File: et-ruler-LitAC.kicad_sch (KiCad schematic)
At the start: 26 parts, among them J1 Conn_01x03, SW1 SW_DPST

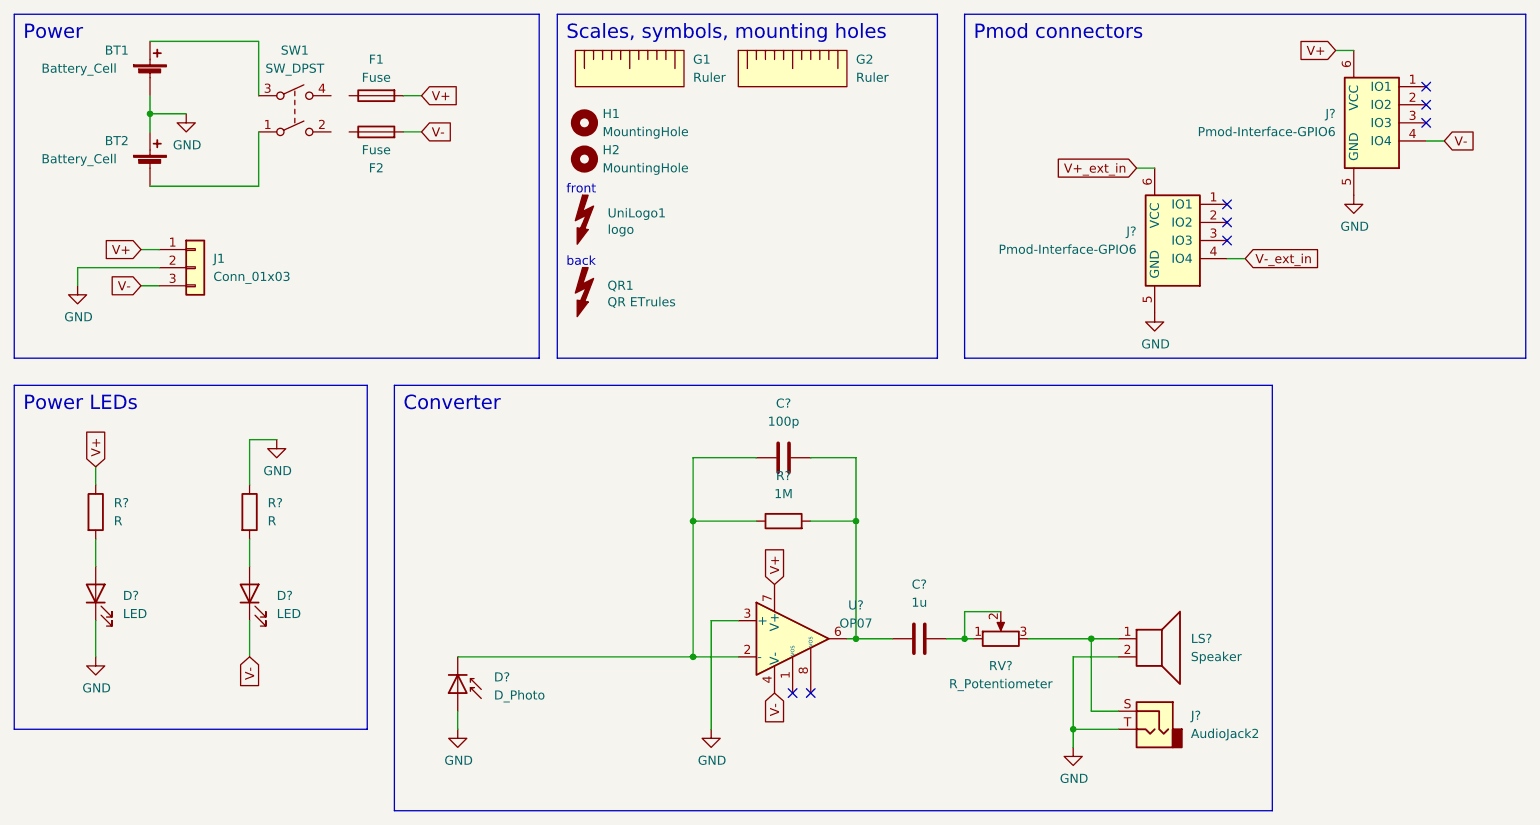
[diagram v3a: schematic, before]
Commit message: Add PCB from template
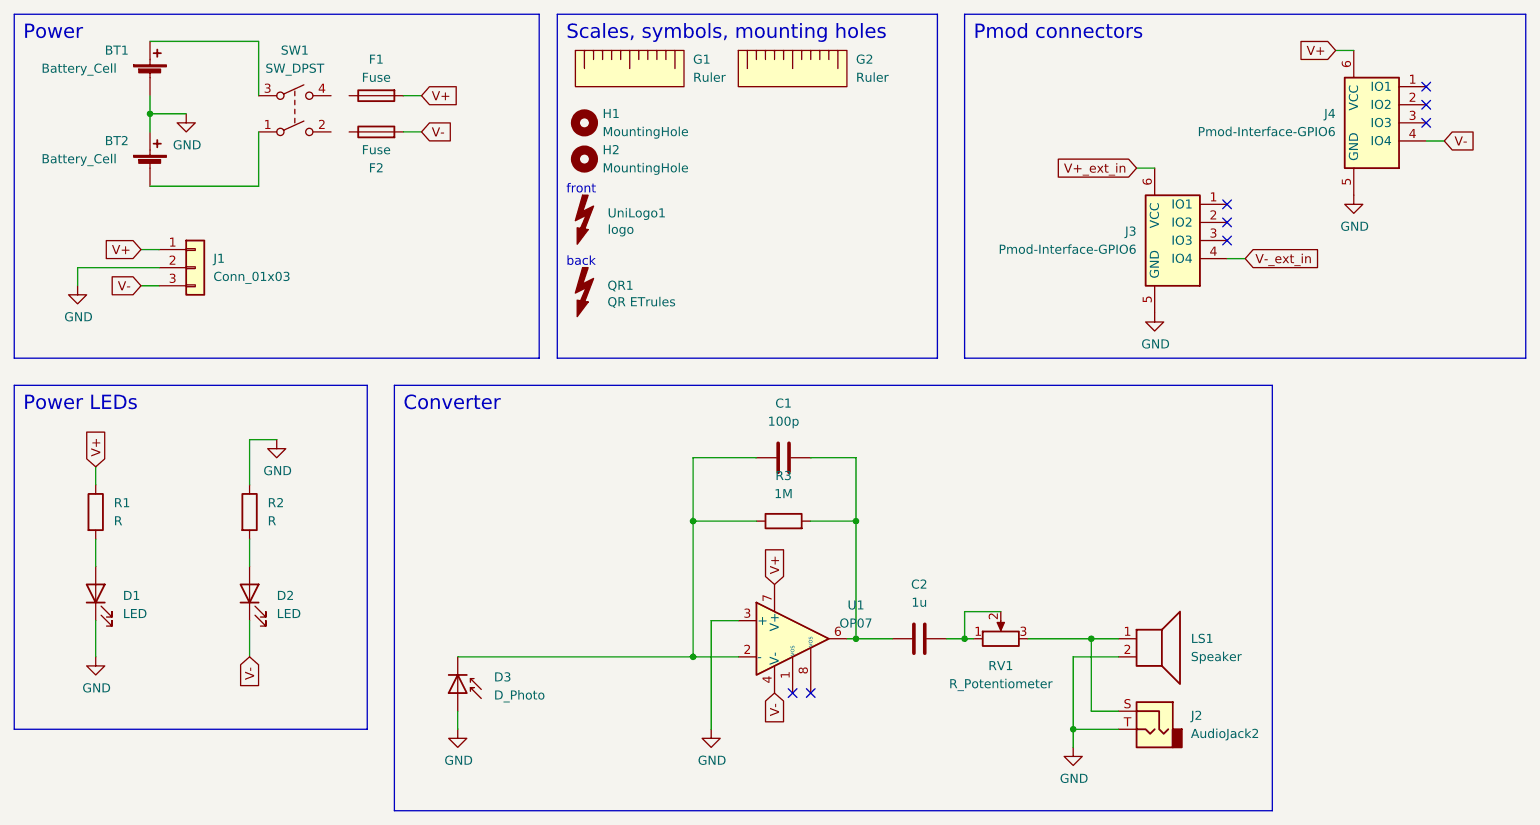
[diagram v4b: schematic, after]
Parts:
- gave numbers to parts that had none: 14

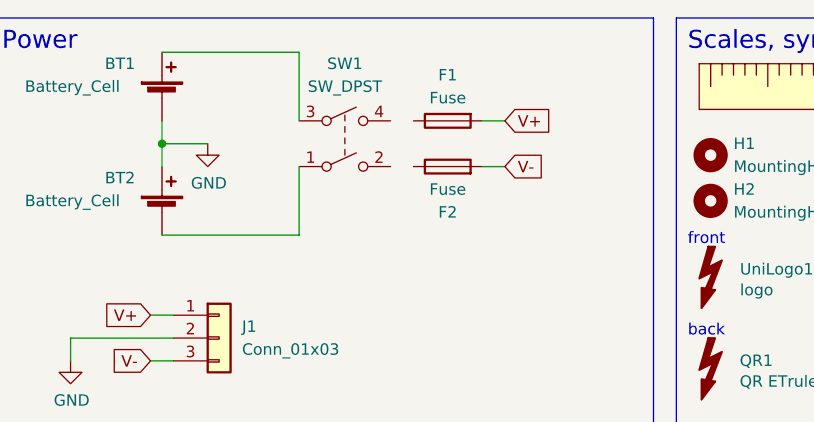
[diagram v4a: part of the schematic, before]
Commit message: Add correct switch symbol and footprint
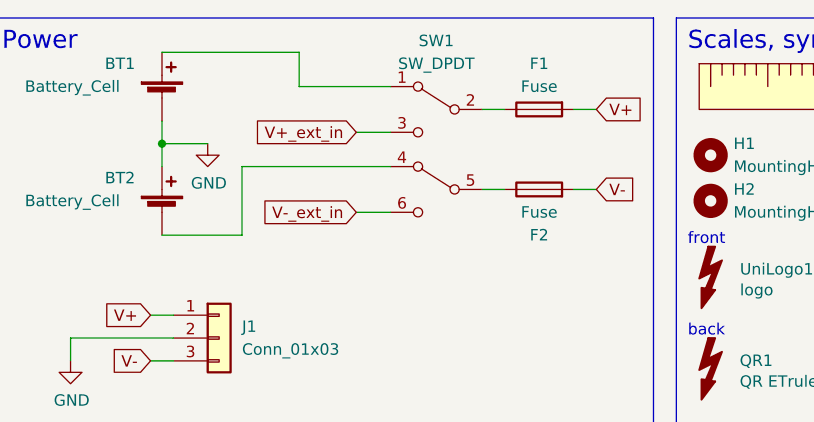
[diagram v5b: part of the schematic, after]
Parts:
- removed SW1: SW_DPST, symbol Switch:SW_DPST
- added SW1: SW_DPDT, Switch-HYBRID-emt:Switch_DPDT_SMD_THT_Hybrid, symbol et-ruler-symbols:SW_DPDT
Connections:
- net V+_ext_in: now also SW1.3 (C)
- net V-_ext_in: now also SW1.6 (F)
- net at BT2.2 (-): now also SW1.4 (D)
- net at BT1.1 (+): now also SW1.1 (A)
- net at F1.1: now also SW1.2 (B)
- net at F2.1: now also SW1.5 (E)
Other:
- moved on the sheet: F1, F2
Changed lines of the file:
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@@
-    (stroke (width 0) (type default) (color 0 0 0 0))
-  )
-  (wire (pts (xy 52.07 21.59) (xy 52.07 29.21))
     (stroke (width 0) (type default) (color 0 0 0 0))
   )
@@
     (stroke (width 0) (type default) (color 0 0 0 0))
   )
+  (wire (pts (xy 82.55 36.83) (xy 85.09 36.83))
+    (stroke (width 0) (type default) (color 0 0 0 0))
+  )
   (wire (pts (xy 35.56 55.88) (xy 38.1 55.88))
     (stroke (width 0) (type default) (color 0 0 0 0))
@@
     (stroke (width 0) (type default) (color 0 0 0 0))
   )
+  (wire (pts (xy 72.39 36.83) (xy 74.93 36.83))
+    (stroke (width 0) (type default) (color 0 0 0 0))
+  )
   (polyline (pts (xy 17.78 69.85) (xy 17.78 118.11))
     (stroke (width 0) (type default) (color 0 0 0 0))
@@
     (stroke (width 0) (type default) (color 0 0 0 0))
   )
+  (wire (pts (xy 72.39 27.94) (xy 74.93 27.94))
+    (stroke (width 0) (type default) (color 0 0 0 0))
+  )
   (wire (pts (xy 119.38 102.87) (xy 115.57 102.87))
     (stroke (width 0) (type default) (color 0 0 0 0))
@@
     (stroke (width 0) (type default) (color 0 0 0 0))
   )
+  (wire (pts (xy 45.72 41.91) (xy 45.72 34.29))
+    (stroke (width 0) (type default) (color 0 0 0 0))
+  )
   (polyline (pts (xy 67.31 118.11) (xy 67.31 69.85))
     (stroke (width 0) (type default) (color 0 0 0 0))
@@
     (stroke (width 0) (type default) (color 0 0 0 0))
   )
+  (wire (pts (xy 52.07 25.4) (xy 62.23 25.4))
+    (stroke (width 0) (type default) (color 0 0 0 0))
+  )
   (wire (pts (xy 166.37 118.11) (xy 172.72 118.11))
     (stroke (width 0) (type default) (color 0 0 0 0))
@@
     (stroke (width 0) (type default) (color 0 0 0 0))
   )
+  (wire (pts (xy 36.83 41.91) (xy 45.72 41.91))
+    (stroke (width 0) (type default) (color 0 0 0 0))
+  )
   (wire (pts (xy 80.01 115.57) (xy 80.01 118.11))
     (stroke (width 0) (type default) (color 0 0 0 0))
@@
     (stroke (width 0) (type default) (color 0 0 0 0))
   )
+  (wire (pts (xy 82.55 27.94) (xy 85.09 27.94))
+    (stroke (width 0) (type default) (color 0 0 0 0))
+  )
   (wire (pts (xy 168.91 105.41) (xy 172.72 105.41))
     (stroke (width 0) (type default) (color 0 0 0 0))
@@
     (stroke (width 0) (type default) (color 0 0 0 0))
   )
-  (wire (pts (xy 36.83 41.91) (xy 52.07 41.91))
+  (wire (pts (xy 62.23 30.48) (xy 58.42 30.48))
     (stroke (width 0) (type default) (color 0 0 0 0))
   )
@@
     (stroke (width 0) (type default) (color 0 0 0 0))
   )
-  (wire (pts (xy 52.07 41.91) (xy 52.07 34.29))
+  (wire (pts (xy 52.07 21.59) (xy 52.07 25.4))
     (stroke (width 0) (type default) (color 0 0 0 0))
   )
@@
     (stroke (width 0) (type default) (color 0 0 0 0))
   )
-  (wire (pts (xy 72.39 29.21) (xy 74.93 29.21))
-    (stroke (width 0) (type default) (color 0 0 0 0))
-  )
   (polyline (pts (xy 91.44 66.04) (xy 91.44 17.78))
     (stroke (width 0) (type default) (color 0 0 0 0))
@@
     (stroke (width 0) (type default) (color 0 0 0 0))
   )
+  (wire (pts (xy 62.23 39.37) (xy 58.42 39.37))
+    (stroke (width 0) (type default) (color 0 0 0 0))
+  )
   (wire (pts (xy 135.89 105.41) (xy 140.97 105.41))
     (stroke (width 0) (type default) (color 0 0 0 0))
@@
     (stroke (width 0) (type default) (color 0 0 0 0))
   )
-  (wire (pts (xy 72.39 34.29) (xy 74.93 34.29))
-    (stroke (width 0) (type default) (color 0 0 0 0))
-  )
   (wire (pts (xy 29.21 91.44) (xy 29.21 95.25))
     (stroke (width 0) (type default) (color 0 0 0 0))
@@
   )
   (wire (pts (xy 36.83 31.75) (xy 36.83 34.29))
+    (stroke (width 0) (type default) (color 0 0 0 0))
+  )
+  (wire (pts (xy 45.72 34.29) (xy 62.23 34.29))
     (stroke (width 0) (type default) (color 0 0 0 0))
   )
@@
     (effects (font (size 2 2)) (justify left bottom))
   )
-  (global_label "V+" (shape input) (at 74.93 29.21 0) (fields_autoplaced)
+  (global_label "V+" (shape input) (at 85.09 27.94 0) (fields_autoplaced)
     (effects (font (size 1.27 1.27)) (justify left))
-    (property "Intersheet References" "${INTERSHEET_REFS}" (id 0) (at 80.0041 29.1306 0)
+    (property "Intersheet References" "${INTERSHEET_REFS}" (id 0) (at 90.1641 27.8606 0)
       (effects (font (size 1.27 1.27)) (justify left) hide)
     )
@@
     )
   )
-  (global_label "V-" (shape input) (at 74.93 34.29 0) (fields_autoplaced)
+  (global_label "V-" (shape input) (at 85.09 36.83 0) (fields_autoplaced)
     (effects (font (size 1.27 1.27)) (justify left))
-    (property "Intersheet References" "${INTERSHEET_REFS}" (id 0) (at 80.0041 34.2106 0)
+    (property "Intersheet References" "${INTERSHEET_REFS}" (id 0) (at 90.1641 36.7506 0)
       (effects (font (size 1.27 1.27)) (justify left) hide)
     )
@@
     )
   )
+  (global_label "V+_ext_in" (shape input) (at 58.42 30.48 180) (fields_autoplaced)
+    (effects (font (size 1.27 1.27)) (justify right))
+    (property "Intersheet References" "${INTERSHEET_REFS}" (id 0) (at 46.8145 30.5594 0)
+      (effects (font (size 1.27 1.27)) (justify right) hide)
+    )
+  )
+  (global_label "V-_ext_in" (shape input) (at 58.42 39.37 180) (fields_autoplaced)
+    (effects (font (size 1.27 1.27)) (justify right))
+    (property "Intersheet References" "${INTERSHEET_REFS}" (id 0) (at 46.8145 39.2906 0)
+      (effects (font (size 1.27 1.27)) (justify right) hide)
+    )
+  )
   (global_label "V+" (shape input) (at 124.46 97.79 90) (fields_autoplaced)
     (effects (font (size 1.27 1.27)) (justify left))
@@
     )
   )
-  (symbol (lib_id "Switch:SW_DPST") (at 57.15 31.75 0) (unit 1)
-    (in_bom yes) (on_board yes) (fields_autoplaced)
-    (property "Reference" "SW1" (id 0) (at 57.15 22.86 0))
-    (property "Value" "SW_DPST" (id 1) (at 57.15 25.4 0))
-    (property "Footprint" "" (id 2) (at 57.15 31.75 0)
-      (effects (font (size 1.27 1.27)) hide)
-    )
-    (property "Datasheet" "~" (id 3) (at 57.15 31.75 0)
-      (effects (font (size 1.27 1.27)) hide)
-    )
-    (pin "1")
-    (pin "2")
-    (pin "3")
-    (pin "4")
-  )
   (symbol (lib_id "Connector_Generic:Conn_01x03") (at 43.18 53.34 0) (unit 1)
     (in_bom yes) (on_board yes) (fields_autoplaced)
@@
     (pin "2")
   )
-  (symbol (lib_id "Device:Fuse") (at 68.58 29.21 90) (mirror x) (unit 1)
-    (in_bom yes) (on_board yes)
-    (property "Reference" "F1" (id 0) (at 68.58 24.13 90))
-    (property "Value" "Fuse" (id 1) (at 68.58 26.67 90))
-    (property "Footprint" "et-ruler-footprints:R_0805_THT_5.08mm_Hybrid" (id 2) (at 68.58 27.432 90)
-      (effects (font (size 1.27 1.27)) hide)
-    )
-    (property "Datasheet" "~" (id 3) (at 68.58 29.21 0)
+  (symbol (lib_id "Device:Fuse") (at 78.74 27.94 90) (mirror x) (unit 1)
+    (in_bom yes) (on_board yes)
+    (property "Reference" "F1" (id 0) (at 78.74 22.86 90))
+    (property "Value" "Fuse" (id 1) (at 78.74 25.4 90))
+    (property "Footprint" "et-ruler-footprints:R_0805_THT_5.08mm_Hybrid" (id 2) (at 78.74 26.162 90)
+      (effects (font (size 1.27 1.27)) hide)
+    )
+    (property "Datasheet" "~" (id 3) (at 78.74 27.94 0)
       (effects (font (size 1.27 1.27)) hide)
     )
@@
     (pin "1")
   )
+  (symbol (lib_id "et-ruler-symbols:SW_DPDT") (at 67.31 33.02 0) (mirror y) (unit 1)
+    (in_bom yes) (on_board yes) (fields_autoplaced)
+    (property "Reference" "SW1" (id 0) (at 67.31 20.32 0))
+    (property "Value" "SW_DPDT" (id 1) (at 67.31 22.86 0))
+    (property "Footprint" "Switch-HYBRID-emt:Switch_DPDT_SMD_THT_Hybrid" (id 2) (at 67.31 27.94 0)
+      (effects (font (size 1.27 1.27)) hide)
+    )
+    (property "Datasheet" "~" (id 3) (at 67.31 27.94 0)
+      (effects (font (size 1.27 1.27)) hide)
+    )
+    (property "THT" "https://www.mouser.de/ProductDetail/CK/JS202011CQN?qs=LgMIjt8LuD%2Fe%252BE3iTcEFYw%3D%3D" (id 4) (at 67.31 33.02 0)
+      (effects (font (size 1.27 1.27)) hide)
+    )
+    (pin "1")
+    (pin "2")
+    (pin "3")
+    (pin "4")
+    (pin "5")
+    (pin "6")
+  )
   (symbol (lib_id "Device:R_Potentiometer") (at 156.21 105.41 90) (unit 1)
     (in_bom yes) (on_board yes) (fields_autoplaced)
@@
     (pin "2")
   )
-  (symbol (lib_id "Device:Fuse") (at 68.58 34.29 90) (unit 1)
-    (in_bom yes) (on_board yes)
-    (property "Reference" "F2" (id 0) (at 68.58 39.37 90))
-    (property "Value" "Fuse" (id 1) (at 68.58 36.83 90))
-    (property "Footprint" "et-ruler-footprints:R_0805_THT_5.08mm_Hybrid" (id 2) (at 68.58 36.068 90)
-      (effects (font (size 1.27 1.27)) hide)
-    )
-    (property "Datasheet" "~" (id 3) (at 68.58 34.29 0)
+  (symbol (lib_id "Device:Fuse") (at 78.74 36.83 90) (unit 1)
+    (in_bom yes) (on_board yes)
+    (property "Reference" "F2" (id 0) (at 78.74 41.91 90))
+    (property "Value" "Fuse" (id 1) (at 78.74 39.37 90))
+    (property "Footprint" "et-ruler-footprints:R_0805_THT_5.08mm_Hybrid" (id 2) (at 78.74 38.608 90)
+      (effects (font (size 1.27 1.27)) hide)
+    )
+    (property "Datasheet" "~" (id 3) (at 78.74 36.83 0)
       (effects (font (size 1.27 1.27)) hide)
     )
@@
       (reference "RV1") (unit 1) (value "R_Potentiometer") (footprint "")
     )
-    (path "/0c91bcd3-285e-47fd-acbd-2bedce603d40"
-      (reference "SW1") (unit 1) (value "SW_DPST") (footprint "")
+    (path "/a9c8deae-344f-43f2-9a96-00809bd843b5"
+      (reference "SW1") (unit 1) (value "SW_DPDT") (footprint "Switch-HYBRID-emt:Switch_DPDT_SMD_THT_Hybrid")
     )
     (path "/dcceaca1-a887-4411-b23c-e33d2f2afa8b"

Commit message: Fix DPDT switch footprint
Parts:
- SW1: footprint Switch-HYBRID-emt:Switch_DPDT_SMD_THT_Hybrid -> Switch-HYBRID-emt:Switch_DPDT_SMD_THT_Hybrid_P2.54; SMD_Mouser (none) -> https://www.mouser.de/ProductDetail/CK/JS202011SCQN?qs=LgMI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; THT https://www.mouser.de/ProductDetail/CK/JS202011CQN?qs=LgMIj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 -> (none); THT_Reichelt (none) -> https://www.reichelt.de/schiebeschalter-gerade-rm2-54-2x-ei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
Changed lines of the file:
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@@
     (property "Reference" "SW1" (id 0) (at 67.31 20.32 0))
     (property "Value" "SW_DPDT" (id 1) (at 67.31 22.86 0))
-    (property "Footprint" "Switch-HYBRID-emt:Switch_DPDT_SMD_THT_Hybrid" (id 2) (at 67.31 27.94 0)
+    (property "Footprint" "Switch-HYBRID-emt:Switch_DPDT_SMD_THT_Hybrid_P2.54" (id 2) (at 67.31 27.94 0)
       (effects (font (size 1.27 1.27)) hide)
     )
@@
       (effects (font (size 1.27 1.27)) hide)
     )
-    (property "THT" "https://www.mouser.de/ProductDetail/CK/JS202011CQN?qs=LgMIjt8LuD%2Fe%252BE3iTcEFYw%3D%3D" (id 4) (at 67.31 33.02 0)
+    (property "THT_Reichelt" "https://www.reichelt.de/schiebeschalter-gerade-rm2-54-2x-ein-ein-ss-25146-nh-p105711.html?&trstct=pol_9&nbc=1" (id 5) (at 67.31 33.02 0)
+      (effects (font (size 1.27 1.27)) hide)
+    )
+    (property "SMD_Mouser" "https://www.mouser.de/ProductDetail/CK/JS202011SCQN?qs=LgMIjt8LuD95JYWxZ7NvZA%3D%3D" (id 5) (at 67.31 33.02 0)
       (effects (font (size 1.27 1.27)) hide)
     )
@@
     )
     (path "/a9c8deae-344f-43f2-9a96-00809bd843b5"
-      (reference "SW1") (unit 1) (value "SW_DPDT") (footprint "Switch-HYBRID-emt:Switch_DPDT_SMD_THT_Hybrid")
+      (reference "SW1") (unit 1) (value "SW_DPDT") (footprint "Switch-HYBRID-emt:Switch_DPDT_SMD_THT_Hybrid_P2.54")
     )
     (path "/dcceaca1-a887-4411-b23c-e33d2f2afa8b"

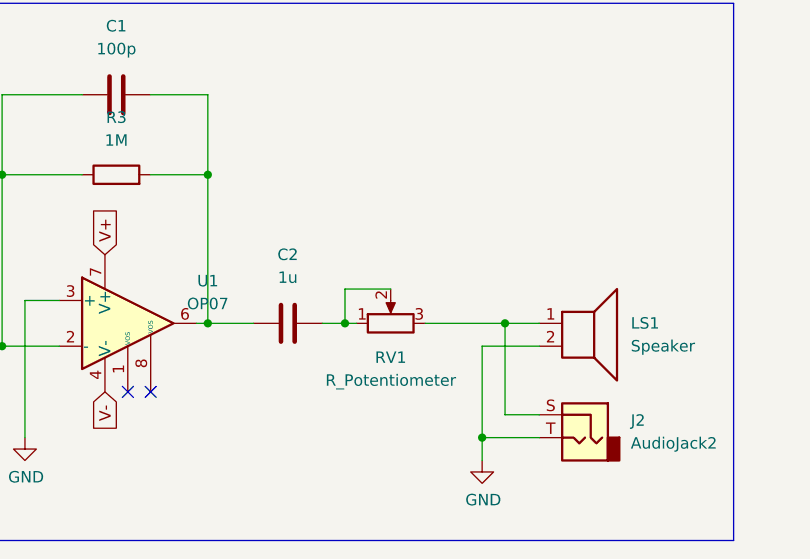
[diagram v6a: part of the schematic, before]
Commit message: Add several footprints
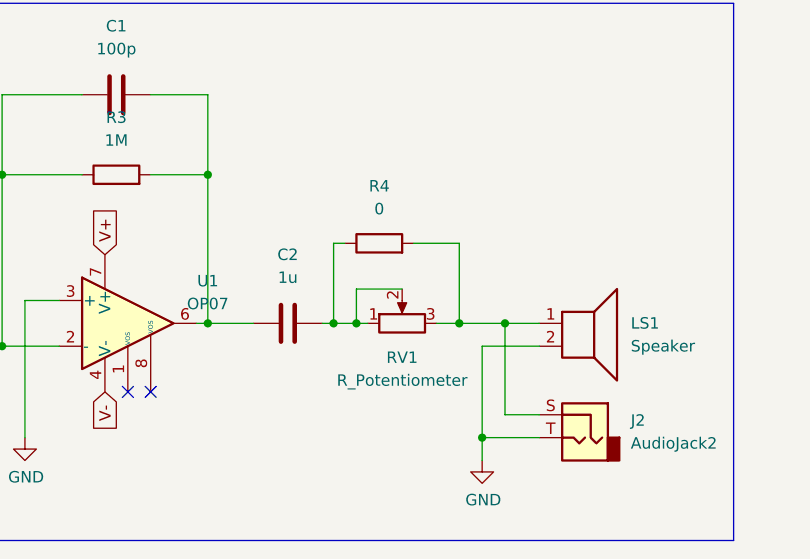
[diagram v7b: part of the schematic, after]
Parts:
- added R4: 0, Resistor_HYBRID-emt:R_0805_THT_10.16mm_Hybrid, symbol Device:R
- C1, C2: footprint (none) -> Capacitor_HYBRID-emt:C_0805_THT_5.08mm_Hybrid
- D1, D2: footprint et-ruler-footprints:LED_THT_SMD_Hybrid_D3.0mm -> LED_HYBRID-emt:LED_THT_SMD_Hybrid_D3.0mm
- F1, F2: footprint et-ruler-footprints:R_0805_THT_5.08mm_Hybrid -> Resistor_HYBRID-emt:R_0805_THT_5.08mm_Hybrid
- R1, R2: footprint et-ruler-footprints:R_0805_THT_10.16mm_Hybrid -> Resistor_HYBRID-emt:R_0805_THT_10.16mm_Hybrid
- R3: footprint (none) -> Resistor_HYBRID-emt:R_0805_THT_10.16mm_Hybrid
- RV1: footprint (none) -> Potentiometer_THT:Potentiometer_ACP_CA14V-15_Vertical
- U1: footprint Package_DIP:DIP-8_W7.62mm_Socket_LongPads -> Package_HYBRID-emt:DIP_SMDIP-8_W7.62mm_Socket
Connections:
- net at C2.2, RV1.1, RV1.2: now also R4.1
- net at J2.S, LS1.1, RV1.3: now also R4.2
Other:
- moved on the sheet: RV1
